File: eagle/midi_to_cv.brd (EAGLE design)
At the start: 100 x 80 mm, 66 parts, among them IC1 4093N, Q3 2N3904, Q4 2N3904, Q5 2N3904, Q6 2SK30, U1 ATMEGA328P_PDIP

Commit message: routed
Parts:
- D1: device SparkFun-DiscreteSemi:DIODE-1N4148 -> SparkFun-DiscreteSemi:DIODE-1N4148-KIT
- R1: device rcl:0204/5 -> rcl:0204/7
- R12: device rcl:0207/15 -> rcl:0207/12
- moved Q5 12.7 mm to (76.2, 31.8)
- moved PAD12 8.13 mm to (26.2, 67.6)
- moved MB 4.58 mm to (57.1, 69.8), turned to 90 degrees
- moved R13 2.03 mm to (74.2, 26.7)
- moved R18 1.85 mm to (18.5, 12.2)
- moved C13 1.83 mm to (87.9, 21.3)
- moved D1 1.63 mm to (75.2, 24.1)
- moved OUTPUT 1.44 mm to (87.9, 13.0)
- moved C12 1.30 mm to (82.5, 12.4)
- moved C11 1.27 mm to (82.5, 16.5)
- moved R22 1.27 mm to (26.0, 53.0)
- moved U$4 0.76 mm to (78.2, 60.8)
- moved R1 0.57 mm to (27.2, 64.0)
- moved D3 0.51 mm to (79.5, 20.3)
- moved R3 0.25 mm to (15.0, 21.6)
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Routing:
- net RETURN: track 280.2 -> 235.3 mm, vias 0 -> 2
- net +5V: track 136.2 -> 179.9 mm, vias 0 -> 4
- net +12V: track 157.2 -> 189.6 mm, vias 0 -> 4
- net GND: track 445.5 -> 424.8 mm
- net N$16: track 24.0 -> 11.9 mm
- net N$11: track 37.5 -> 47.4 mm
- net N$1: track 9.69 -> 15.4 mm
- net N$21: track 10.0 -> 6.22 mm
- net CB_TRIG: track 22.4 -> 25.7 mm
- net N$15: track 12.0 -> 14.3 mm
- net N$32: track 20.8 -> 22.9 mm
- net N$22: track 11.1 -> 12.8 mm
- net N$17: track 21.2 -> 22.5 mm
- net NOISE: track 76.0 -> 77.3 mm
- net N$29: track 23.2 -> 24.3 mm
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
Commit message: tweaks
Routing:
- net CB_TRIG: track 25.7 -> 24.5 mm
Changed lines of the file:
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@@
 <wire x1="100" y1="80" x2="0" y2="80" width="0" layer="20"/>
 <wire x1="0" y1="80" x2="0" y2="0" width="0" layer="20"/>
+<rectangle x1="84.582" y1="58.928" x2="88.646" y2="65.532" layer="16"/>
 </plain>
 <attributes>
@@
 <contactref element="C1" pad="2"/>
 <contactref element="R15" pad="2"/>
-<wire x1="32.004" y1="40.005" x2="32.004" y2="38.4048" width="0.6604" layer="16"/>
-<wire x1="32.004" y1="38.4048" x2="32.004" y2="37.0713" width="0.6604" layer="16"/>
+<wire x1="32.004" y1="40.005" x2="32.004" y2="38.4048" width="0.8128" layer="16"/>
+<wire x1="32.004" y1="38.4048" x2="32.004" y2="37.0713" width="0.8128" layer="16"/>
 <wire x1="32.5374" y1="40.5384" x2="32.004" y2="40.005" width="0.6604" layer="16"/>
 <wire x1="32.004" y1="37.0713" x2="31.877" y2="36.83" width="0.6604" layer="16"/>
 <wire x1="32.5374" y1="40.5384" x2="32.766" y2="40.64" width="0.6604" layer="16"/>
 <wire x1="30.6705" y1="42.672" x2="30.6705" y2="43.2054" width="0.6604" layer="16"/>
-<wire x1="32.5374" y1="40.8051" x2="30.6705" y2="42.672" width="0.6604" layer="16"/>
+<wire x1="32.5374" y1="40.8051" x2="30.6705" y2="42.672" width="0.8128" layer="16"/>
 <wire x1="30.6705" y1="43.2054" x2="30.48" y2="43.434" width="0.6604" layer="16"/>
 <wire x1="32.5374" y1="40.8051" x2="32.766" y2="40.64" width="0.6604" layer="16"/>
@@
 <wire x1="25.3365" y1="40.5384" x2="25.146" y2="40.64" width="0.6604" layer="16"/>
 <wire x1="33.8201" y1="35.7378" x2="36.8046" y2="35.7378" width="0.8128" layer="16"/>
-<wire x1="33.2867" y1="35.2044" x2="33.8201" y2="35.7378" width="0.6604" layer="16"/>
+<wire x1="33.2867" y1="35.2044" x2="33.8201" y2="35.7378" width="0.8128" layer="16"/>
 <wire x1="28.5369" y1="35.2044" x2="33.2867" y2="35.2044" width="0.8128" layer="16"/>
 <wire x1="27.2034" y1="36.5379" x2="28.5369" y2="35.2044" width="0.8128" layer="16"/>
@@
 <wire x1="31.115" y1="63.7413" x2="30.988" y2="64.008" width="0.6604" layer="16"/>
 <wire x1="36.8046" y1="58.674" x2="36.83" y2="58.674" width="0.6604" layer="16"/>
-<wire x1="31.4579" y1="63.9953" x2="33.7947" y2="63.9953" width="0.8128" layer="16"/>
-<wire x1="33.7947" y1="63.9953" x2="36.83" y2="58.674" width="0.8128" layer="16"/>
+<wire x1="31.4579" y1="63.9953" x2="33.5407" y2="63.9953" width="0.8128" layer="16"/>
+<wire x1="33.5407" y1="63.9953" x2="36.83" y2="58.674" width="0.8128" layer="16"/>
 <wire x1="30.988" y1="64.008" x2="29.21" y2="64.516" width="0.8128" layer="16"/>
 <wire x1="29.21" y1="64.516" x2="26.162" y2="67.564" width="0.8128" layer="16"/>
@@
 <wire x1="70.4088" y1="67.7418" x2="70.485" y2="67.564" width="0.6604" layer="16"/>
 <wire x1="48.5394" y1="72.2757" x2="48.26" y2="72.39" width="0.6604" layer="16"/>
-<wire x1="28.5369" y1="43.4721" x2="28.0035" y2="43.4721" width="0.6604" layer="16"/>
-<wire x1="29.3751" y1="45.0723" x2="28.5369" y2="43.4721" width="0.8128" layer="16"/>
-<wire x1="31.2039" y1="45.0723" x2="29.3751" y2="45.0723" width="0.8128" layer="16"/>
-<wire x1="32.8041" y1="43.4721" x2="31.2039" y2="45.0723" width="0.8128" layer="16"/>
+<wire x1="28.2829" y1="43.4721" x2="28.0035" y2="43.4721" width="0.6604" layer="16"/>
+<wire x1="29.1211" y1="45.0723" x2="28.2829" y2="43.4721" width="0.8128" layer="16"/>
+<wire x1="31.9659" y1="45.0723" x2="29.1211" y2="45.0723" width="0.8128" layer="16"/>
+<wire x1="32.8041" y1="43.4721" x2="31.9659" y2="45.0723" width="0.8128" layer="16"/>
 <wire x1="28.0035" y1="43.4721" x2="27.94" y2="43.434" width="0.6604" layer="16"/>
 <wire x1="32.8041" y1="43.4721" x2="33.02" y2="43.434" width="0.6604" layer="16"/>
@@
 <contactref element="U1" pad="5"/>
 <wire x1="41.0718" y1="51.2699" x2="37.0713" y2="48.5394" width="0.6604" layer="16"/>
-<wire x1="41.0718" y1="64.5668" x2="41.0718" y2="51.2699" width="0.6604" layer="16"/>
-<wire x1="45.8724" y1="64.5414" x2="41.0718" y2="64.5668" width="0.6604" layer="16"/>
+<wire x1="41.0718" y1="63.2968" x2="41.0718" y2="51.2699" width="0.6604" layer="16"/>
+<wire x1="45.8724" y1="64.5414" x2="41.0718" y2="63.2968" width="0.6604" layer="16"/>
 <wire x1="48.006" y1="64.5414" x2="45.8724" y2="64.5414" width="0.6604" layer="16"/>
 <wire x1="37.0713" y1="48.5394" x2="36.83" y2="48.514" width="0.6604" layer="16"/>

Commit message: tweaks
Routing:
- net +12V: track 189.6 -> 186.7 mm
- net GND: track 425.1 -> 424.6 mm
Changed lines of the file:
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@@
 <wire x1="87.63" y1="45.72" x2="84.0105" y2="49.3395" width="0.8128" layer="16"/>
 <wire x1="84.0105" y1="50.673" x2="83.82" y2="50.8" width="0.6604" layer="16"/>
-<wire x1="72.2757" y1="56.8071" x2="69.8754" y2="56.8071" width="0.8128" layer="16"/>
-<wire x1="73.6092" y1="58.1406" x2="72.2757" y2="56.8071" width="0.8128" layer="16"/>
+<wire x1="71.7677" y1="57.3151" x2="69.8754" y2="56.8071" width="0.8128" layer="16"/>
+<wire x1="73.6092" y1="58.1406" x2="71.7677" y2="57.3151" width="0.8128" layer="16"/>
 <wire x1="69.8754" y1="56.8071" x2="69.85" y2="56.642" width="0.6604" layer="16"/>
 <wire x1="73.6092" y1="58.1406" x2="73.66" y2="58.166" width="0.6604" layer="16"/>
@@
 <wire x1="60.96" y1="31.75" x2="60.96" y2="36.068" width="0.8128" layer="16"/>
 <via x="60.96" y="36.068" extent="1-16" drill="0.8" shape="square"/>
-<wire x1="60.96" y1="36.068" x2="60.96" y2="39.878" width="0.8128" layer="1"/>
-<wire x1="60.96" y1="39.878" x2="54.864" y2="40.132" width="0.8128" layer="1"/>
+<wire x1="60.96" y1="36.068" x2="57.658" y2="38.354" width="0.8128" layer="1"/>
+<wire x1="57.658" y1="38.354" x2="54.864" y2="40.132" width="0.8128" layer="1"/>
 <via x="54.864" y="40.132" extent="1-16" drill="0.8" shape="square"/>
 <wire x1="54.864" y1="40.132" x2="58.42" y2="42.418" width="0.8128" layer="16"/>
@@
 <wire x1="60.8076" y1="44.5389" x2="60.96" y2="44.45" width="0.6604" layer="16"/>
 <wire x1="58.4073" y1="51.7398" x2="58.42" y2="52.07" width="0.6604" layer="16"/>
-<wire x1="59.7408" y1="60.2742" x2="60.9346" y2="62.484" width="0.8128" layer="16"/>
+<wire x1="59.7408" y1="60.2742" x2="60.9346" y2="61.976" width="0.8128" layer="16"/>
 <wire x1="59.7408" y1="60.0075" x2="59.7408" y2="60.2742" width="0.6604" layer="16"/>
 <wire x1="59.7408" y1="60.0075" x2="59.69" y2="59.69" width="0.6604" layer="16"/>
@@
 <wire x1="37.8714" y1="6.1341" x2="38.1" y2="6.35" width="0.6604" layer="16"/>
 <wire x1="22.9362" y1="4.5339" x2="22.86" y2="5.08" width="0.6604" layer="16"/>
-<wire x1="89.662" y1="27.8384" x2="89.0778" y2="28.6766" width="0.8128" layer="16"/>
+<wire x1="89.662" y1="27.8384" x2="89.5858" y2="29.4386" width="0.8128" layer="16"/>
 <wire x1="89.662" y1="15.1638" x2="89.662" y2="27.8384" width="0.8128" layer="16"/>
 <wire x1="89.3953" y1="13.3731" x2="89.662" y2="15.1638" width="0.8128" layer="16"/>
@@
 <wire x1="88.265" y1="39.9923" x2="86.4489" y2="39.9923" width="0.8128" layer="16"/>
 <wire x1="89.6493" y1="39.37" x2="88.265" y2="39.9923" width="0.8128" layer="16"/>
-<wire x1="89.6493" y1="32.258" x2="89.6493" y2="39.37" width="0.8128" layer="16"/>
-<wire x1="89.0778" y1="30.6705" x2="89.6493" y2="32.258" width="0.8128" layer="16"/>
+<wire x1="89.6493" y1="33.528" x2="89.6493" y2="39.37" width="0.8128" layer="16"/>
+<wire x1="89.0778" y1="31.9405" x2="89.6493" y2="33.528" width="0.8128" layer="16"/>
 <wire x1="72.5424" y1="45.0596" x2="72.39" y2="44.45" width="0.6604" layer="16"/>
-<wire x1="89.0778" y1="30.6705" x2="88.897221875" y2="30.667828125" width="0.6604" layer="16"/>
-<wire x1="88.897221875" y1="30.667828125" x2="82.362171875" y2="30.667828125" width="0.8128" layer="16"/>
-<wire x1="82.362171875" y1="30.667828125" x2="81.28" y2="31.75" width="0.8128" layer="16"/>
+<wire x1="89.0778" y1="31.9405" x2="88.897221875" y2="31.683828125" width="0.6604" layer="16"/>
+<wire x1="88.897221875" y1="31.683828125" x2="82.362171875" y2="31.683828125" width="0.8128" layer="16"/>
+<wire x1="82.362171875" y1="31.683828125" x2="81.28" y2="31.75" width="0.8128" layer="16"/>
 <wire x1="81.28" y1="31.75" x2="78.74" y2="31.75" width="0.8128" layer="16"/>
 <wire x1="78.74" y1="31.75" x2="76.2" y2="30.48" width="0.8128" layer="16"/>
@@
 <wire x1="35.7378" y1="6.1341" x2="35.7378" y2="7.7216" width="0.8128" layer="16"/>
 <wire x1="26.9367" y1="30.4038" x2="26.67" y2="30.48" width="0.6604" layer="16"/>
-<wire x1="60.9346" y1="62.484" x2="65.024" y2="65.278" width="0.8128" layer="16"/>
-<wire x1="65.024" y1="65.278" x2="65.024" y2="67.056" width="0.8128" layer="16"/>
+<wire x1="60.9346" y1="61.976" x2="65.024" y2="64.77" width="0.8128" layer="16"/>
+<wire x1="65.024" y1="64.77" x2="65.024" y2="67.056" width="0.8128" layer="16"/>
 <wire x1="65.024" y1="67.056" x2="65.024" y2="68.072" width="0.8128" layer="16"/>
 <wire x1="65.024" y1="68.072" x2="64.7446" y2="70.6374" width="0.8128" layer="16"/>
 <wire x1="64.7446" y1="70.6374" x2="64.2366" y2="71.4883" width="0.8128" layer="16"/>
-<wire x1="64.2366" y1="71.4883" x2="63.5" y2="72.2757" width="0.8128" layer="16"/>
+<wire x1="64.2366" y1="71.4883" x2="62.992" y2="72.0217" width="0.8128" layer="16"/>
 <wire x1="48.5394" y1="72.2757" x2="57.0357" y2="72.2757" width="0.8128" layer="16"/>
 <wire x1="57.0357" y1="72.2757" x2="57.15" y2="72.39" width="0.8128" layer="16"/>
-<wire x1="57.15" y1="72.39" x2="63.3349" y2="72.39" width="0.8128" layer="16"/>
-<wire x1="63.3349" y1="72.39" x2="64.2366" y2="71.4883" width="0.8128" layer="16"/>
+<wire x1="57.15" y1="72.39" x2="62.3189" y2="72.39" width="0.8128" layer="16"/>
+<wire x1="62.3189" y1="72.39" x2="64.2366" y2="71.4883" width="0.8128" layer="16"/>
 <wire x1="70.4088" y1="67.7418" x2="65.7098" y2="67.7418" width="0.8128" layer="16"/>
 <wire x1="65.7098" y1="67.7418" x2="65.024" y2="67.056" width="0.8128" layer="16"/>
-<wire x1="89.0778" y1="28.6766" x2="89.0778" y2="30.48725" width="0.8128" layer="16"/>
-<wire x1="89.0778" y1="30.48725" x2="88.897221875" y2="30.667828125" width="0.8128" layer="16"/>
+<wire x1="89.5858" y1="29.4386" x2="89.3318" y2="30.48725" width="0.8128" layer="16"/>
+<wire x1="89.3318" y1="30.48725" x2="88.897221875" y2="31.683828125" width="0.8128" layer="16"/>
 <wire x1="72.2757" y1="28.8036" x2="74.5236" y2="28.8036" width="0.8128" layer="16"/>
 <wire x1="74.5236" y1="28.8036" x2="76.2" y2="30.48" width="0.8128" layer="16"/>
@@
 <wire x1="35.4838" y1="29.8577" x2="36.5506" y2="30.9245" width="0.6604" layer="16"/>
 <wire x1="35.2171" y1="29.6037" x2="35.4838" y2="29.8577" width="0.6604" layer="16"/>
-<wire x1="34.671" y1="28.8036" x2="35.2171" y2="29.6037" width="0.6604" layer="16"/>
-<wire x1="34.671" y1="25.0698" x2="34.671" y2="28.8036" width="0.6604" layer="16"/>
+<wire x1="34.671" y1="29.3116" x2="35.2171" y2="29.6037" width="0.6604" layer="16"/>
+<wire x1="34.671" y1="25.0698" x2="34.671" y2="29.3116" width="0.6604" layer="16"/>
 <wire x1="37.8714" y1="21.8694" x2="34.671" y2="25.0698" width="0.6604" layer="16"/>
 <wire x1="40.005" y1="21.8694" x2="37.8714" y2="21.8694" width="0.6604" layer="16"/>
@@
 <contactref element="SD" pad="1"/>
 <contactref element="U1" pad="17"/>
-<wire x1="49.3395" y1="28.1305" x2="44.5389" y2="30.6705" width="0.8128" layer="16"/>
+<wire x1="49.3395" y1="28.1305" x2="45.8089" y2="30.6705" width="0.8128" layer="16"/>
 <wire x1="55.88" y1="24.13" x2="49.3395" y2="28.1305" width="0.8128" layer="16"/>
-<wire x1="44.5389" y1="30.6705" x2="44.45" y2="30.734" width="0.6604" layer="16"/>
+<wire x1="45.8089" y1="30.6705" x2="44.45" y2="30.734" width="0.6604" layer="16"/>
 </signal>
 <signal name="CY_TRIG">
@@
 <contactref element="R3" pad="1"/>
 <contactref element="MIDI_THRU_1" pad="3"/>
-<wire x1="15.2146" y1="14.4653" x2="15.2146" y2="17.6022" width="0.8128" layer="16"/>
-<wire x1="18.4785" y1="11.9634" x2="15.2146" y2="14.4653" width="0.8128" layer="16"/>
+<wire x1="14.9606" y1="14.7193" x2="14.9606" y2="17.6022" width="0.8128" layer="16"/>
+<wire x1="18.4785" y1="11.9634" x2="14.9606" y2="14.7193" width="0.8128" layer="16"/>
 <wire x1="20.0025" y1="5.6007" x2="18.4785" y2="11.9634" width="0.8128" layer="16"/>
 <wire x1="20.2692" y1="5.334" x2="20.0025" y2="5.6007" width="0.6604" layer="16"/>
-<wire x1="15.2146" y1="17.6022" x2="14.986" y2="17.78" width="0.6604" layer="16"/>
+<wire x1="14.9606" y1="17.6022" x2="14.986" y2="17.78" width="0.6604" layer="16"/>
 <wire x1="20.2692" y1="5.334" x2="20.32" y2="5.08" width="0.6604" layer="16"/>
 </signal>

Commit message: tweaks
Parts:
- moved C5 1.78 mm to (74.3, 71.9)
- moved C7 1.27 mm to (70.5, 71.4)
- moved U$5 1.27 mm to (78.2, 72.0)
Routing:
- net GND: track 424.6 -> 426.9 mm
- net RETURN: track 235.3 -> 234.8 mm
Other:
- board size 100 x 80 mm -> 100 x 80.8 mm

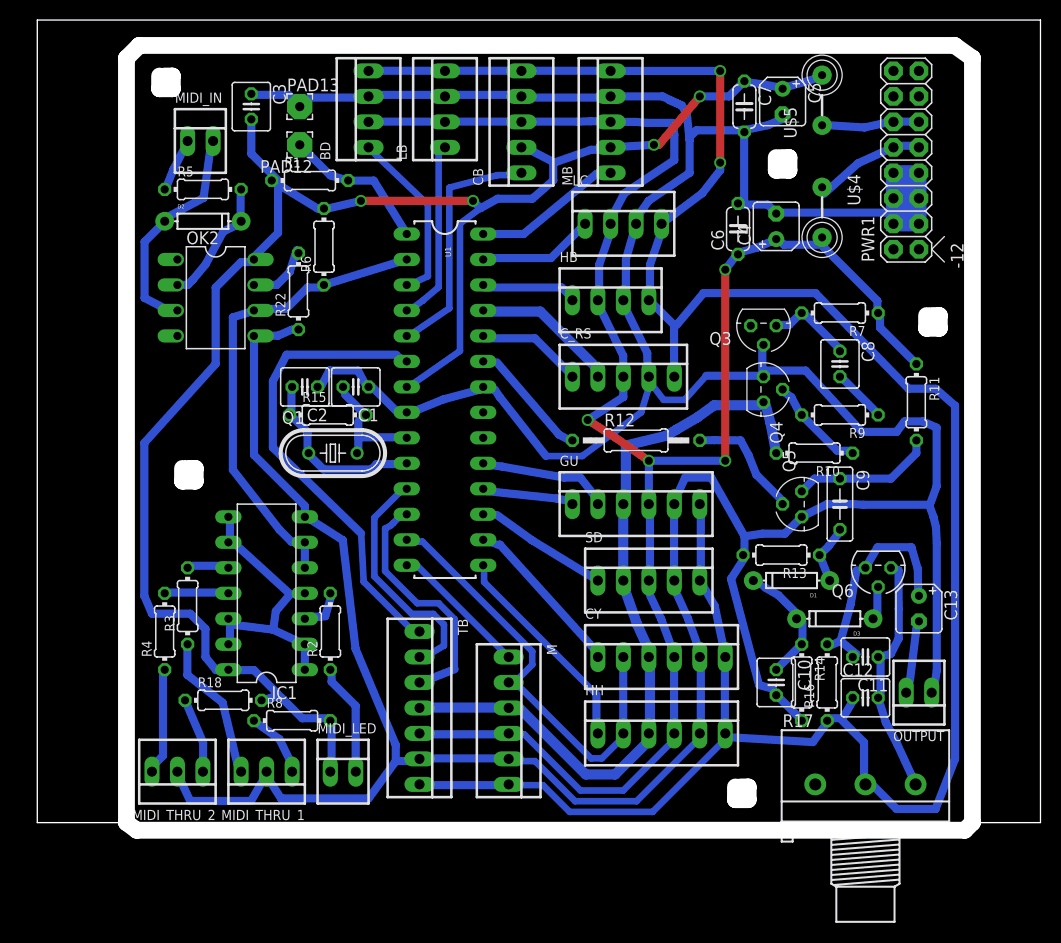
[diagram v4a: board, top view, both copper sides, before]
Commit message: arduino code compiles
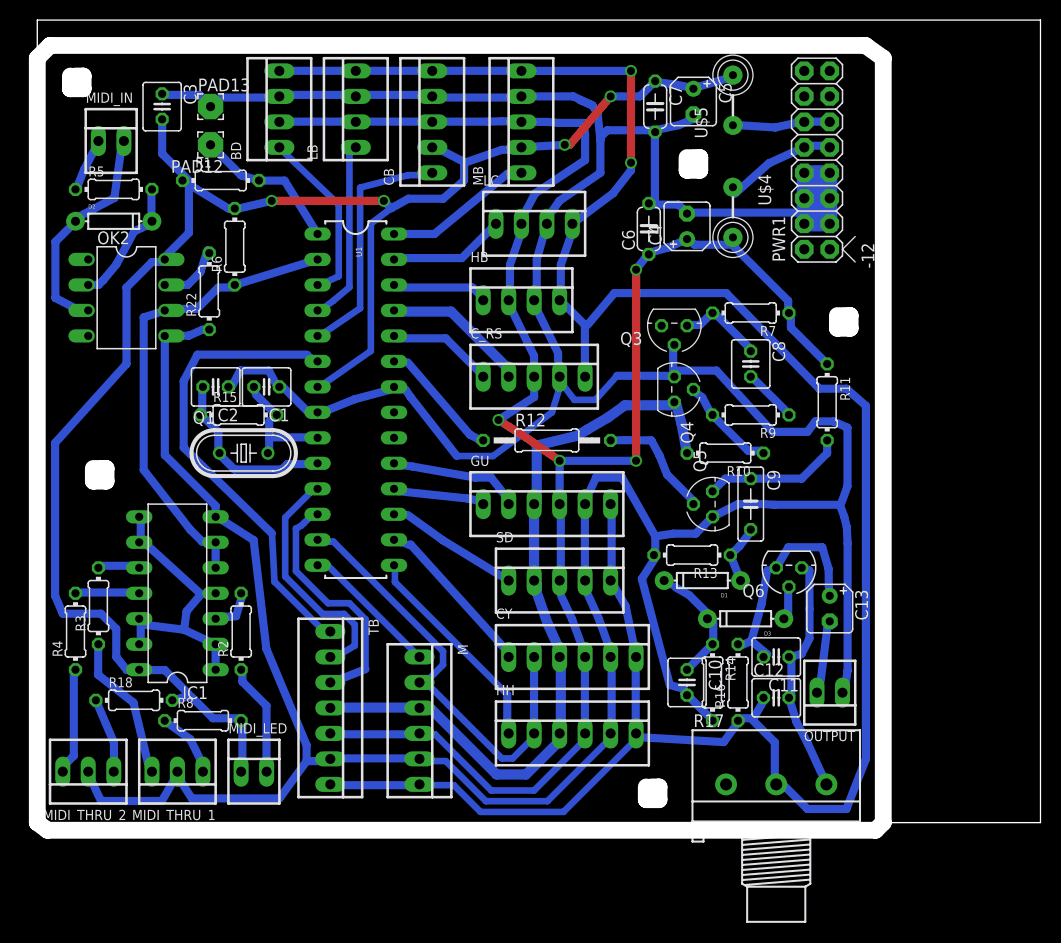
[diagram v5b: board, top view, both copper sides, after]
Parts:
- C8: value 470pF -> 10n
- R10: value 1M5 -> 2M2
- R9: value 68k -> 100k
- moved BD 8.89 mm to (24.1, 71.1)
- moved R18 8.89 mm to (9.65, 12.2)
- moved C1 8.89 mm to (22.9, 43.4)
- moved C10 8.89 mm to (64.8, 14.0)
- moved C11 8.89 mm to (73.7, 16.5)
- moved C12 8.89 mm to (73.7, 12.4)
- moved C13 8.89 mm to (79.0, 21.3)
- moved C2 8.89 mm to (17.8, 43.4)
- moved C4 8.89 mm to (64.8, 59.4)
- moved C5 8.89 mm to (65.4, 71.9)
- moved C7 8.89 mm to (61.6, 71.4)
- moved C8 8.89 mm to (71.1, 45.7)
- moved C9 8.89 mm to (71.1, 31.8)
- moved CB 8.89 mm to (39.4, 69.8)
- moved C_RS 8.89 mm to (49.5, 44.5)
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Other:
- outline, holes or cut-outs redrawn
